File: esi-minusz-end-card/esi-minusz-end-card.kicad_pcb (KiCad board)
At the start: 4 copper layers, 99.8 x 94.6 mm, 86 parts, among them J1 J-SAMTEC-TFM-120-01-L-D-RA, J2 U.FL-R-SMT-1, J3 M55-7101242R, J4 M55-7101242R, J5 M55-7101242R, J6 +UHF, J7 -UHF, J8 M55-7101242R, Q1 DMP2240UDM, Q2 PMV45EN, Q3 PMV45EN, Q4 PMV45EN, Q5 DMP2240UDM-7, Q6 PMV45EN, Q7 DMP2240UDM-7, U1 NCS2-62+, U11 MIC842LYC5, U12 MIC842LYC5, U2 MAX7310, U201 TS5A21366, U202 TS5A21366, U203 TS5A21366, U204 TS5A21366

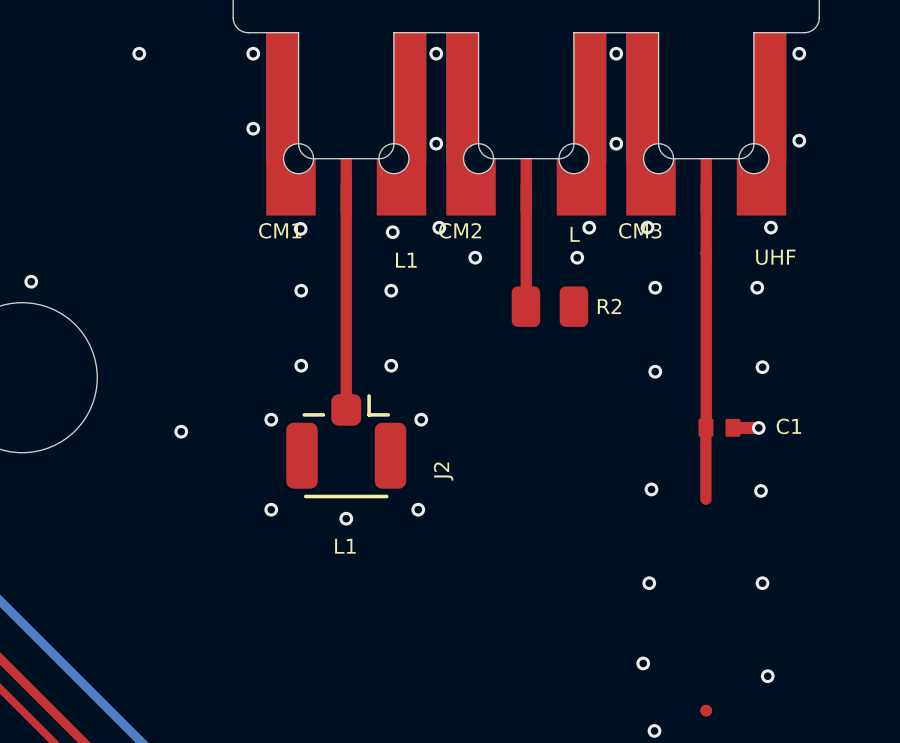
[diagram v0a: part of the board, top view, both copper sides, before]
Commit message: Swapped L and L1 Bands
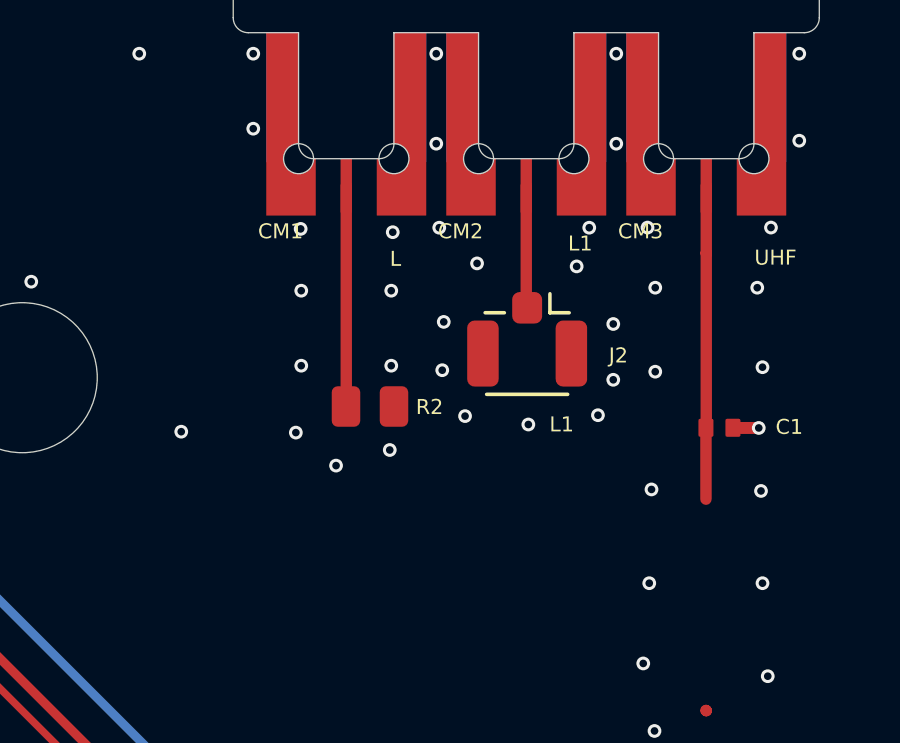
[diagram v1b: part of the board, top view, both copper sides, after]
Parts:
- moved J2 6.92 mm to (176.5, 72.4)
- moved R2 6.86 mm to (171.3, 74.2)
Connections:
- CM1 pad SIG: /L1BAND -> /LBAND
- CM2 pad SIG: /LBAND -> /L1BAND
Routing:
- net /L1BAND: track 7.55 -> 4.10 mm
- net /LBAND: track 4.03 -> 7.36 mm
- net GND: vias 356 -> 361
